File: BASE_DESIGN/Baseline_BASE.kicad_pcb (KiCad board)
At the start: 2 copper layers, 103.6 x 38.2 mm, 24 parts, among them J1 PinSocket_1x04_P2.00mm_Vertic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, J2 PinSocket_1x04_P2.00mm_Vertic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, J4 PinSocket_1x04_P2.00mm_Vertic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, J5 PinSocket_1x04_P2.00mm_Vertic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

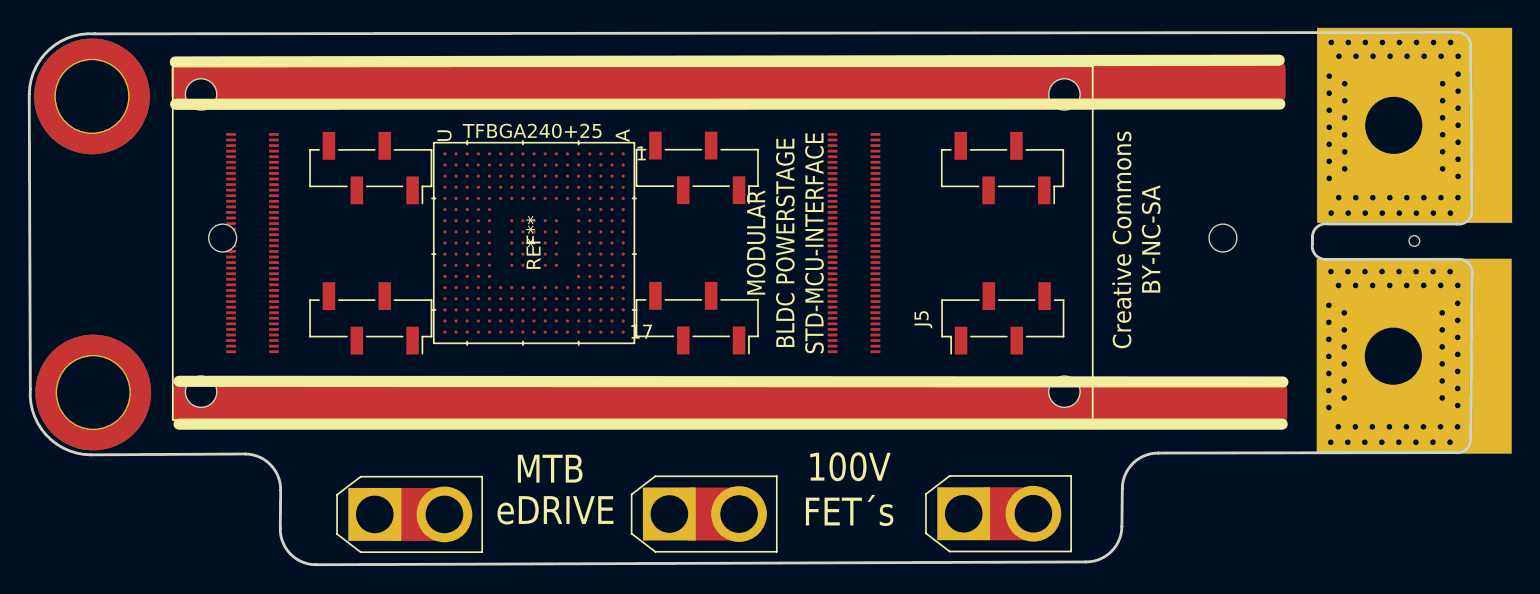
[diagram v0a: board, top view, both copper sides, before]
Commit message: Moved header
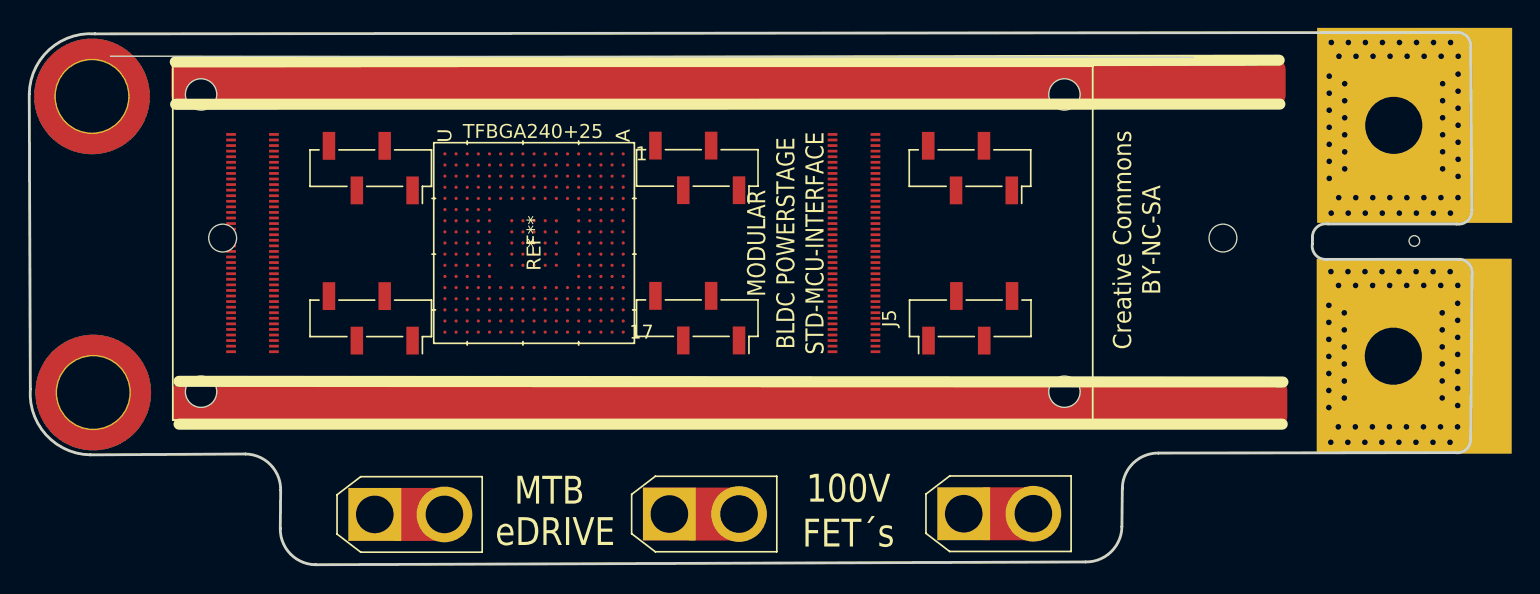
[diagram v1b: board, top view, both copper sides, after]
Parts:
- moved J5 2.34 mm to (160.8, 92.4)
- moved J2 2.34 mm to (160.8, 81.7)
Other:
- outline, holes or cut-outs redrawn
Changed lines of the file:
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@@
   )
   (footprint "Connector_PinSocket_2.00mm:PinSocket_1x04_P2.00mm_Vertical_SMD_Pin1Right" (layer "F.Cu")
-    (at 163.105 81.66 -90)
+    (at 160.77 81.655217 -90)
     (descr "surface-mounted straight socket strip, 1x04, 2.00mm pitch, single row, style 2 (pin 1 right) (https://www.jayconsystems.com/fileuploader/download/download/?d=1&file=custom%2Fupload%2FFile-1375728122.pdf), script generated")
     (tags "Surface mounted socket strip SMD 1x04 2.00mm single row style2 pin1 right")
@@
   )
   (footprint "Connector_PinSocket_2.00mm:PinSocket_1x04_P2.00mm_Vertical_SMD_Pin1Left" (layer "F.Cu")
-    (at 163.125 92.444783 90)
+    (at 160.79 92.44 90)
     (descr "surface-mounted straight socket strip, 1x04, 2.00mm pitch, single row, style 1 (pin 1 left) (https://www.jayconsystems.com/fileuploader/download/download/?d=1&file=custom%2Fupload%2FFile-1375728122.pdf), script generated")
     (tags "Surface mounted socket strip SMD 1x04 2.00mm single row style1 pin1 left")
@@
   (gr_line (start 97.954907 72.020927) (end 195.7 71.92) (layer "Edge.Cuts") (width 0.2))
   (gr_arc (start 185.355352 86.6773) (mid 185.67 85.9) (end 186.475352 85.6673) (layer "Edge.Cuts") (width 0.2))
+  (gr_line (start 99.067228 73.621646) (end 176.825 73.707791) (layer "Edge.Cuts") (width 0.1))
   (gr_arc (start 195.8027 88.205352) (mid 196.58 88.52) (end 196.8127 89.325352) (layer "Edge.Cuts") (width 0.2))
   (gr_arc (start 97.632737 102.24363) (mid 94.452608 100.817307) (end 93.312737 97.52363) (layer "Edge.Cuts") (width 0.2))
@@
   (gr_line (start 93.234907 76.340927) (end 93.312737 97.52363) (layer "Edge.Cuts") (width 0.2))
   (gr_line (start 196.8 84.66) (end 196.71 73.04) (layer "Edge.Cuts") (width 0.2))
-  (gr_text "eDRIVE" (at 131.02 106.28) (layer "F.SilkS")
+  (gr_text "eDRIVE" (at 130.99 107.79) (layer "F.SilkS")
     (effects (font (size 2 1.7) (thickness 0.425)))
   )
-  (gr_text "100V\nFET´s" (at 152.07 104.78) (layer "F.SilkS")
+  (gr_text "100V\nFET´s" (at 152.04 106.29) (layer "F.SilkS")
     (effects (font (size 2 1.7) (thickness 0.425)))
   )
-  (gr_text "MTB" (at 130.6 103.31) (layer "F.SilkS")
+  (gr_text "MTB" (at 130.57 104.82) (layer "F.SilkS")
     (effects (font (size 2 1.7) (thickness 0.425)))
   )
